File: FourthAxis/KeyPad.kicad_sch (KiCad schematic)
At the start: 49 parts, among them SW1 SW_Push, SW10 SW_Push, SW11 SW_Push, SW12 SW_Push, SW13 SW_Push, SW14 SW_Push, SW15 SW_Push, SW16 SW_Push, SW17 SW_Push, SW18 SW_Push, SW19 SW_Push, SW2 SW_Push, SW20 SW_Push, SW21 SW_Push, SW22 SW_Push, SW3 SW_Push, SW4 SW_Push, SW5 SW_Push, SW6 SW_Push, SW7 SW_Push, SW8 SW_Push, SW9 SW_Push, U2 74HC237

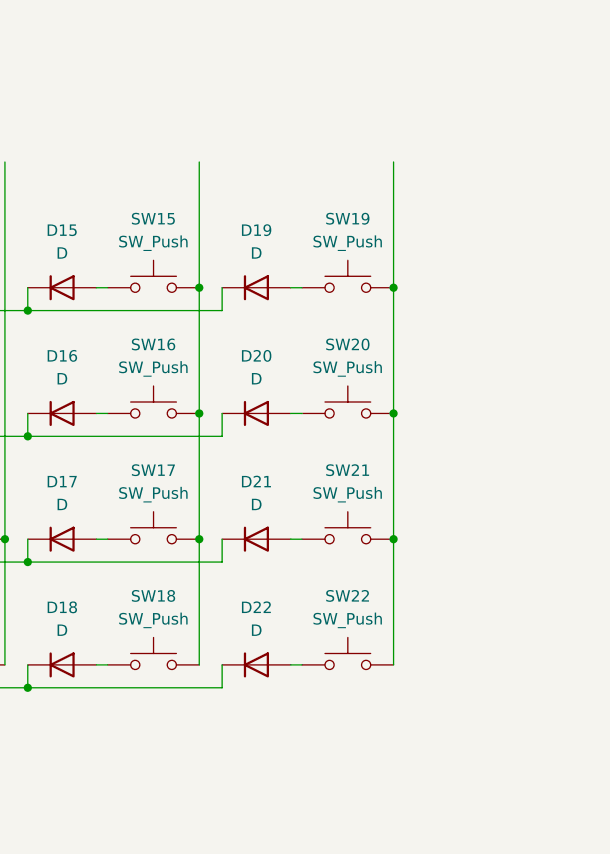
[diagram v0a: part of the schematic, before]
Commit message: Added handwheel sheet
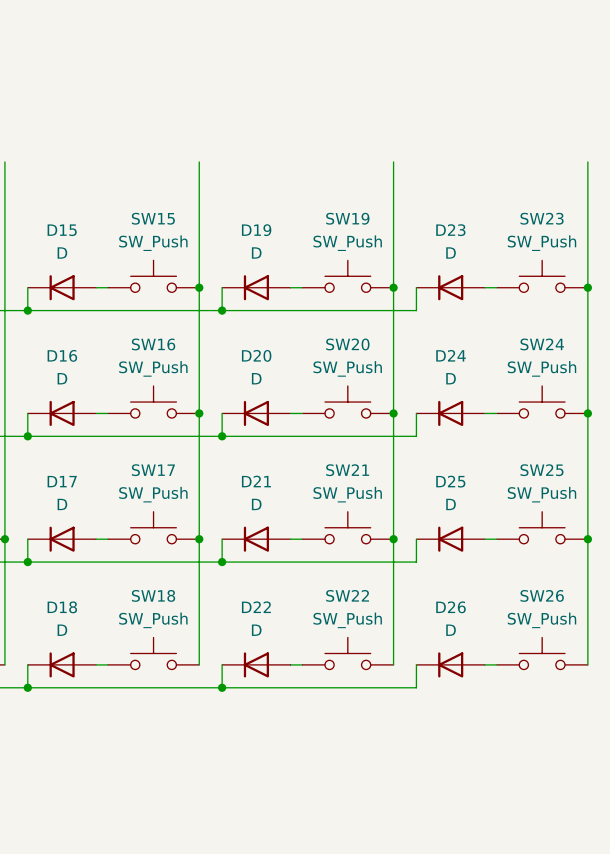
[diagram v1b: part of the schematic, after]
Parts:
- added D23, D24, D25, D26: D, symbol Device:D
- added SW23, SW24, SW25, SW26: SW_Push, symbol Switch:SW_Push
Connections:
- net at D12.1 (K), D14.1 (K), D18.1 (K)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: now also D26.1 (K)
- net at D11.1 (K), D13.1 (K), D17.1 (K)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: now also D25.1 (K)
- net at D1.1 (K), D15.1 (K), D19.1 (K)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: now also D23.1 (K)
- net at D10.1 (K), D16.1 (K), D2.1 (K)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: now also D24.1 (K)
- new net: D23.2 (A), SW23.1
- new net: D24.2 (A), SW24.1
- new net: D25.2 (A), SW25.1
- new net: D26.2 (A), SW26.1
- new net: SW23.2, SW24.2, SW25.2, SW26.2

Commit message: Keypad schem work
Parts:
- added R10, R7, R8, R9: 10k, Resistor_SMD:R_0603_1608Metric, symbol Device:R_US
- D1, D10, D11, D12, D13, D14, D15, D16, D17, D18, D19, D2, D20, D21, D22, D23, D24, D25, D26, D3, D4, D5, D6, D7, D8, D9: footprint (none) -> Diode_SMD:D_SOD-323
- R1, R2, R3, R4: footprint (none) -> Resistor_SMD:R_0603_1608Metric
- SW1, SW10, SW11, SW12, SW13, SW14, SW15, SW16, SW17, SW18, SW19, SW2, SW20, SW21, SW22, SW23, SW24, SW25, SW26, SW3, SW4, SW5, SW6, SW7, SW8, SW9: footprint (none) -> Button_Switch_Keyboard:SW_Cherry_MX_1.00u_PCB
- U2: footprint (none) -> Package_SO:SOIC-16_3.9x9.9mm_P1.27mm; Digikey Part Number (none) -> 74HC237DCT-ND
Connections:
- net GND: now also U2.8 (GND), R10.2, R7.2, R8.2
- net at SW13.2, SW14.2: now also U2.12 (Y3)
- net at SW19.2, SW20.2, SW21.2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: now also U2.10 (Y5)
- net KEY_4: now reaches D12.1 (K), D14.1 (K), D18.1 (K), D22.1 (K), D26.1 (K), D4.1 (K), D8.1 (K), R4.1
- net KEY_A: now reaches U2.1 (A0)
- net at U2.11 (Y4): now also SW15.2, SW16.2, SW17.2, SW18.2
- net at U2.13 (Y2): now also SW10.2, SW11.2, SW12.2, SW9.2
- net at U2.14 (Y1): now also SW5.2, SW6.2, SW7.2, SW8.2
- net at U2.15 (Y0): now also SW1.2, SW2.2, SW3.2, SW4.2
- net 3V3: now reaches U2.16 (VCC)
- net 3V3: now also R9.1
- net KEY_B: now reaches U2.2 (A1)
- net KEY_C: now reaches U2.3 (A2)
- net at U2.4 (~{LE}): now also R8.1
- net at U2.5 (~{E1}): now also R7.1
- net at U2.6 (E2): now also R9.2
- net at U2.7 (Y7): now also R10.1
- net at U2.9 (Y6): now also SW23.2, SW24.2, SW25.2, SW26.2
- net KEY_3: now reaches D11.1 (K), D13.1 (K), D17.1 (K), D21.1 (K), D25.1 (K), D3.1 (K), D7.1 (K), R3.1
- net KEY_1: now reaches D1.1 (K), D15.1 (K), D19.1 (K), D23.1 (K), D5.1 (K), D9.1 (K), R1.1
- net KEY_2: now reaches D10.1 (K), D16.1 (K), D2.1 (K), D20.1 (K), D24.1 (K), D6.1 (K), R2.1
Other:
- moved on the sheet: U2

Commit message: schem additions
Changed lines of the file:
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@@
 	)
 	(hierarchical_label "KEY_3"
-		(shape input)
+		(shape output)
 		(at 68.58 110.49 180)
 		(effects
@@
 	)
 	(hierarchical_label "KEY_1"
-		(shape input)
+		(shape output)
 		(at 68.58 82.55 180)
 		(effects
@@
 	)
 	(hierarchical_label "KEY_4"
-		(shape input)
+		(shape output)
 		(at 68.58 124.46 180)
 		(effects
@@
 	)
 	(hierarchical_label "KEY_2"
-		(shape input)
+		(shape output)
 		(at 68.58 96.52 180)
 		(effects

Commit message: name and layout
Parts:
- SW1: value SW_Push -> NUM_1; footprint Button_Switch_Keyboard:SW_Cherry_MX_1.00u_PCB -> CustomFooties:SW_Cherry_MX_1.00u_PCB
- SW10: value SW_Push -> NUM_6; footprint Button_Switch_Keyboard:SW_Cherry_MX_1.00u_PCB -> CustomFooties:SW_Cherry_MX_1.00u_PCB
- SW11: value SW_Push -> NUM_9; footprint Button_Switch_Keyboard:SW_Cherry_MX_1.00u_PCB -> CustomFooties:SW_Cherry_MX_1.00u_PCB
- SW12: value SW_Push -> PLUS_MINUS; footprint Button_Switch_Keyboard:SW_Cherry_MX_1.00u_PCB -> CustomFooties:SW_Cherry_MX_1.00u_PCB
- SW13: value SW_Push -> DELETE; footprint Button_Switch_Keyboard:SW_Cherry_MX_1.00u_PCB -> CustomFooties:SW_Cherry_MX_1.00u_PCB
- SW14: value SW_Push -> ENTER; footprint Button_Switch_Keyboard:SW_Cherry_MX_1.00u_PCB -> CustomFooties:SW_Cherry_MX_1.00u_PCB
- SW15: value SW_Push -> SET_ZERO; footprint Button_Switch_Keyboard:SW_Cherry_MX_1.00u_PCB -> CustomFooties:SW_Cherry_MX_1.00u_PCB
- SW16: value SW_Push -> SET_SPLN; footprint Button_Switch_Keyboard:SW_Cherry_MX_1.00u_PCB -> CustomFooties:SW_Cherry_MX_1.00u_PCB
- SW17: value SW_Push -> ANG_ABS; footprint Button_Switch_Keyboard:SW_Cherry_MX_1.00u_PCB -> CustomFooties:SW_Cherry_MX_1.00u_PCB
- SW18: value SW_Push -> ROT_CCW; footprint Button_Switch_Keyboard:SW_Cherry_MX_1.00u_PCB -> CustomFooties:SW_Cherry_MX_1.00u_PCB
- SW19: value SW_Push -> RET_ZERO; footprint Button_Switch_Keyboard:SW_Cherry_MX_1.00u_PCB -> CustomFooties:SW_Cherry_MX_1.00u_PCB
- SW2: value SW_Push -> NUM_4; footprint Button_Switch_Keyboard:SW_Cherry_MX_1.00u_PCB -> CustomFooties:SW_Cherry_MX_1.00u_PCB
- SW20: value SW_Push -> NXT_SPLN; footprint Button_Switch_Keyboard:SW_Cherry_MX_1.00u_PCB -> CustomFooties:SW_Cherry_MX_1.00u_PCB
- SW21: value SW_Push -> ANG_INC; footprint Button_Switch_Keyboard:SW_Cherry_MX_1.00u_PCB -> CustomFooties:SW_Cherry_MX_1.00u_PCB
- SW22: value SW_Push -> ROT_CW; footprint Button_Switch_Keyboard:SW_Cherry_MX_1.00u_PCB -> CustomFooties:SW_Cherry_MX_1.00u_PCB
- SW23: value SW_Push -> EXTRA_1; footprint Button_Switch_Keyboard:SW_Cherry_MX_1.00u_PCB -> CustomFooties:SW_Cherry_MX_1.00u_PCB
- SW24: value SW_Push -> EXTRA_2; footprint Button_Switch_Keyboard:SW_Cherry_MX_1.00u_PCB -> CustomFooties:SW_Cherry_MX_1.00u_PCB
- SW25: value SW_Push -> EXTRA_3; footprint Button_Switch_Keyboard:SW_Cherry_MX_1.00u_PCB -> CustomFooties:SW_Cherry_MX_1.00u_PCB
- SW26: value SW_Push -> EXTRA_4; footprint Button_Switch_Keyboard:SW_Cherry_MX_1.00u_PCB -> CustomFooties:SW_Cherry_MX_1.00u_PCB
- SW3: value SW_Push -> NUM_7; footprint Button_Switch_Keyboard:SW_Cherry_MX_1.00u_PCB -> CustomFooties:SW_Cherry_MX_1.00u_PCB
- SW4: value SW_Push -> DECIMAL; footprint Button_Switch_Keyboard:SW_Cherry_MX_1.00u_PCB -> CustomFooties:SW_Cherry_MX_1.00u_PCB
- SW5: value SW_Push -> NUM_2; footprint Button_Switch_Keyboard:SW_Cherry_MX_1.00u_PCB -> CustomFooties:SW_Cherry_MX_1.00u_PCB
- SW6: value SW_Push -> NUM_5; footprint Button_Switch_Keyboard:SW_Cherry_MX_1.00u_PCB -> CustomFooties:SW_Cherry_MX_1.00u_PCB
- SW7: value SW_Push -> NUM_8; footprint Button_Switch_Keyboard:SW_Cherry_MX_1.00u_PCB -> CustomFooties:SW_Cherry_MX_1.00u_PCB
- SW8: value SW_Push -> NUM_0; footprint Button_Switch_Keyboard:SW_Cherry_MX_1.00u_PCB -> CustomFooties:SW_Cherry_MX_1.00u_PCB
- SW9: value SW_Push -> NUM_3; footprint Button_Switch_Keyboard:SW_Cherry_MX_1.00u_PCB -> CustomFooties:SW_Cherry_MX_1.00u_PCB
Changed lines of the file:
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@@
 			)
 		)
-		(property "Value" "SW_Push"
+		(property "Value" "DELETE"
 			(at 182.88 102.87 0)
 			(show_name no)
@@
 			)
 		)
-		(property "Footprint" "Button_Switch_Keyboard:SW_Cherry_MX_1.00u_PCB"
+		(property "Footprint" "CustomFooties:SW_Cherry_MX_1.00u_PCB"
 			(at 182.88 102.87 0)
 			(hide yes)
@@
 			)
 		)
-		(property "Value" "SW_Push"
+		(property "Value" "ANG_INC"
 			(at 226.06 102.87 0)
 			(show_name no)
@@
 			)
 		)
-		(property "Footprint" "Button_Switch_Keyboard:SW_Cherry_MX_1.00u_PCB"
+		(property "Footprint" "CustomFooties:SW_Cherry_MX_1.00u_PCB"
 			(at 226.06 102.87 0)
 			(hide yes)
@@
 			)
 		)
-		(property "Value" "SW_Push"
+		(property "Value" "NUM_9"
 			(at 161.29 102.87 0)
 			(show_name no)
@@
 			)
 		)
-		(property "Footprint" "Button_Switch_Keyboard:SW_Cherry_MX_1.00u_PCB"
+		(property "Footprint" "CustomFooties:SW_Cherry_MX_1.00u_PCB"
 			(at 161.29 102.87 0)
 			(hide yes)
@@
 			)
 		)
-		(property "Value" "SW_Push"
+		(property "Value" "RET_ZERO"
 			(at 226.06 74.93 0)
 			(show_name no)
@@
 			)
 		)
-		(property "Footprint" "Button_Switch_Keyboard:SW_Cherry_MX_1.00u_PCB"
+		(property "Footprint" "CustomFooties:SW_Cherry_MX_1.00u_PCB"
 			(at 226.06 74.93 0)
 			(hide yes)
@@
 			)
 		)
-		(property "Value" "SW_Push"
+		(property "Value" "DECIMAL"
 			(at 118.11 116.84 0)
 			(show_name no)
@@
 			)
 		)
-		(property "Footprint" "Button_Switch_Keyboard:SW_Cherry_MX_1.00u_PCB"
+		(property "Footprint" "CustomFooties:SW_Cherry_MX_1.00u_PCB"
 			(at 118.11 116.84 0)
 			(hide yes)
@@
 			)
 		)
-		(property "Value" "SW_Push"
+		(property "Value" "NUM_2"
 			(at 139.7 74.93 0)
 			(show_name no)
@@
 			)
 		)
-		(property "Footprint" "Button_Switch_Keyboard:SW_Cherry_MX_1.00u_PCB"
+		(property "Footprint" "CustomFooties:SW_Cherry_MX_1.00u_PCB"
 			(at 139.7 74.93 0)
 			(hide yes)
@@
 			)
 		)
-		(property "Value" "SW_Push"
+		(property "Value" "NUM_1"
 			(at 118.11 74.93 0)
 			(show_name no)
@@
 			)
 		)
-		(property "Footprint" "Button_Switch_Keyboard:SW_Cherry_MX_1.00u_PCB"
+		(property "Footprint" "CustomFooties:SW_Cherry_MX_1.00u_PCB"
 			(at 118.11 74.93 0)
 			(hide yes)
@@
 			)
 		)
-		(property "Value" "SW_Push"
+		(property "Value" "NUM_8"
 			(at 139.7 102.87 0)
 			(show_name no)
@@
 			)
 		)
-		(property "Footprint" "Button_Switch_Keyboard:SW_Cherry_MX_1.00u_PCB"
+		(property "Footprint" "CustomFooties:SW_Cherry_MX_1.00u_PCB"
 			(at 139.7 102.87 0)
 			(hide yes)
@@
 			)
 		)
-		(property "Value" "SW_Push"
+		(property "Value" "NXT_SPLN"
 			(at 226.06 88.9 0)
 			(show_name no)
@@
 			)
 		)
-		(property "Footprint" "Button_Switch_Keyboard:SW_Cherry_MX_1.00u_PCB"
+		(property "Footprint" "CustomFooties:SW_Cherry_MX_1.00u_PCB"
 			(at 226.06 88.9 0)
 			(hide yes)
@@
 			)
 		)
-		(property "Value" "SW_Push"
+		(property "Value" "ANG_ABS"
 			(at 204.47 102.87 0)
 			(show_name no)
@@
 			)
 		)
-		(property "Footprint" "Button_Switch_Keyboard:SW_Cherry_MX_1.00u_PCB"
+		(property "Footprint" "CustomFooties:SW_Cherry_MX_1.00u_PCB"
 			(at 204.47 102.87 0)
 			(hide yes)
@@
 			)
 		)
-		(property "Value" "SW_Push"
+		(property "Value" "NUM_5"
 			(at 139.7 88.9 0)
 			(show_name no)
@@
 			)
 		)
-		(property "Footprint" "Button_Switch_Keyboard:SW_Cherry_MX_1.00u_PCB"
+		(property "Footprint" "CustomFooties:SW_Cherry_MX_1.00u_PCB"
 			(at 139.7 88.9 0)
 			(hide yes)
@@
 			)
 		)
-		(property "Value" "SW_Push"
+		(property "Value" "ROT_CCW"
 			(at 204.47 116.84 0)
 			(show_name no)
@@
 			)
 		)
-		(property "Footprint" "Button_Switch_Keyboard:SW_Cherry_MX_1.00u_PCB"
+		(property "Footprint" "CustomFooties:SW_Cherry_MX_1.00u_PCB"
 			(at 204.47 116.84 0)
 			(hide yes)
@@
 			)
 		)
-		(property "Value" "SW_Push"
+		(property "Value" "NUM_4"
 			(at 118.11 88.9 0)
 			(show_name no)
@@
 			)
 		)
-		(property "Footprint" "Button_Switch_Keyboard:SW_Cherry_MX_1.00u_PCB"
+		(property "Footprint" "CustomFooties:SW_Cherry_MX_1.00u_PCB"
 			(at 118.11 88.9 0)
 			(hide yes)
@@
 			)
 		)
-		(property "Value" "SW_Push"
+		(property "Value" "EXTRA_2"
 			(at 247.65 88.9 0)
 			(show_name no)
@@
 			)
 		)
-		(property "Footprint" "Button_Switch_Keyboard:SW_Cherry_MX_1.00u_PCB"
+		(property "Footprint" "CustomFooties:SW_Cherry_MX_1.00u_PCB"
 			(at 247.65 88.9 0)
 			(hide yes)
@@
 			)
 		)
-		(property "Value" "SW_Push"
+		(property "Value" "EXTRA_3"
 			(at 247.65 102.87 0)
 			(show_name no)
@@
 			)
 		)
-		(property "Footprint" "Button_Switch_Keyboard:SW_Cherry_MX_1.00u_PCB"
+		(property "Footprint" "CustomFooties:SW_Cherry_MX_1.00u_PCB"
 			(at 247.65 102.87 0)
 			(hide yes)
@@
 			)
 		)
-		(property "Value" "SW_Push"
+		(property "Value" "SET_ZERO"
 			(at 204.47 74.93 0)
 			(show_name no)
@@
 			)
 		)
-		(property "Footprint" "Button_Switch_Keyboard:SW_Cherry_MX_1.00u_PCB"
+		(property "Footprint" "CustomFooties:SW_Cherry_MX_1.00u_PCB"
 			(at 204.47 74.93 0)
 			(hide yes)
@@
 			)
 		)
-		(property "Value" "SW_Push"
+		(property "Value" "NUM_6"
 			(at 161.29 88.9 0)
 			(show_name no)
@@
 			)
 		)
-		(property "Footprint" "Button_Switch_Keyboard:SW_Cherry_MX_1.00u_PCB"
+		(property "Footprint" "CustomFooties:SW_Cherry_MX_1.00u_PCB"
 			(at 161.29 88.9 0)
 			(hide yes)
@@
 			)
 		)
-		(property "Value" "SW_Push"
+		(property "Value" "ROT_CW"
 			(at 226.06 116.84 0)
 			(show_name no)
@@
 			)
 		)
-		(property "Footprint" "Button_Switch_Keyboard:SW_Cherry_MX_1.00u_PCB"
+		(property "Footprint" "CustomFooties:SW_Cherry_MX_1.00u_PCB"
 			(at 226.06 116.84 0)
 			(hide yes)
@@
 			)
 		)
-		(property "Value" "SW_Push"
+		(property "Value" "SET_SPLN"
 			(at 204.47 88.9 0)
 			(show_name no)
@@
 			)
 		)
-		(property "Footprint" "Button_Switch_Keyboard:SW_Cherry_MX_1.00u_PCB"
+		(property "Footprint" "CustomFooties:SW_Cherry_MX_1.00u_PCB"
 			(at 204.47 88.9 0)
 			(hide yes)
@@
 			)
 		)
-		(property "Value" "SW_Push"
+		(property "Value" "NUM_3"
 			(at 161.29 74.93 0)
 			(show_name no)
@@
 			)
 		)
-		(property "Footprint" "Button_Switch_Keyboard:SW_Cherry_MX_1.00u_PCB"
+		(property "Footprint" "CustomFooties:SW_Cherry_MX_1.00u_PCB"
 			(at 161.29 74.93 0)
 			(hide yes)
@@
 			)
 		)
-		(property "Value" "SW_Push"
+		(property "Value" "PLUS_MINUS"
 			(at 161.29 116.84 0)
 			(show_name no)
@@
 			)
 		)
-		(property "Footprint" "Button_Switch_Keyboard:SW_Cherry_MX_1.00u_PCB"
+		(property "Footprint" "CustomFooties:SW_Cherry_MX_1.00u_PCB"
 			(at 161.29 116.84 0)
 			(hide yes)
@@
 			)
 		)
-		(property "Value" "SW_Push"
+		(property "Value" "ENTER"
 			(at 182.88 116.84 0)
 			(show_name no)
@@
 			)
 		)
-		(property "Footprint" "Button_Switch_Keyboard:SW_Cherry_MX_1.00u_PCB"
+		(property "Footprint" "CustomFooties:SW_Cherry_MX_1.00u_PCB"
 			(at 182.88 116.84 0)
 			(hide yes)
@@
 			)
 		)
-		(property "Value" "SW_Push"
+		(property "Value" "NUM_7"
 			(at 118.11 102.87 0)
 			(show_name no)
@@
 			)
 		)
-		(property "Footprint" "Button_Switch_Keyboard:SW_Cherry_MX_1.00u_PCB"
+		(property "Footprint" "CustomFooties:SW_Cherry_MX_1.00u_PCB"
 			(at 118.11 102.87 0)
 			(hide yes)
@@
 			)
 		)
-		(property "Value" "SW_Push"
+		(property "Value" "NUM_0"
 			(at 139.7 116.84 0)
 			(show_name no)
@@
 			)
 		)
-		(property "Footprint" "Button_Switch_Keyboard:SW_Cherry_MX_1.00u_PCB"
+		(property "Footprint" "CustomFooties:SW_Cherry_MX_1.00u_PCB"
 			(at 139.7 116.84 0)
 			(hide yes)
@@
 			)
 		)
-		(property "Value" "SW_Push"
+		(property "Value" "EXTRA_4"
 			(at 247.65 116.84 0)
 			(show_name no)
@@
 			)
 		)
-		(property "Footprint" "Button_Switch_Keyboard:SW_Cherry_MX_1.00u_PCB"
+		(property "Footprint" "CustomFooties:SW_Cherry_MX_1.00u_PCB"
 			(at 247.65 116.84 0)
 			(hide yes)
@@
 			)
 		)
-		(property "Value" "SW_Push"
+		(property "Value" "EXTRA_1"
 			(at 247.65 74.93 0)
 			(show_name no)
@@
 			)
 		)
-		(property "Footprint" "Button_Switch_Keyboard:SW_Cherry_MX_1.00u_PCB"
+		(property "Footprint" "CustomFooties:SW_Cherry_MX_1.00u_PCB"
 			(at 247.65 74.93 0)
 			(hide yes)

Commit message: digikey PN and footprints
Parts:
- D1, D10, D11, D12, D13, D14, D15, D16, D17, D18, D19, D2, D20, D21, D22, D23, D24, D25, D26, D3, D4, D5, D6, D7, D8, D9: footprint Diode_SMD:D_SOD-323 -> Diode_SMD:D_SOD-123; digikey (none) -> 641-1458-1-ND
- R1: renamed from R9; digikey (none) -> 311-10.0KHRCT-ND
- R2: renamed from R8; digikey (none) -> 311-10.0KHRCT-ND
- R3: renamed from R7; digikey (none) -> 311-10.0KHRCT-ND
- R4: renamed from R1; digikey (none) -> 311-10.0KHRCT-ND
- R5: renamed from R10; digikey (none) -> 311-10.0KHRCT-ND
- R6: renamed from R2; digikey (none) -> 311-10.0KHRCT-ND
- R7: renamed from R3; digikey (none) -> 311-10.0KHRCT-ND
- R8: renamed from R4; digikey (none) -> 311-10.0KHRCT-ND
- U2: digikey (none) -> 74HC237DCT-ND
